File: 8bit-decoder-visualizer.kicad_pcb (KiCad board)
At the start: 2 copper layers, 45 parts, among them SW1 SW_SPDT, SW2 SW_SPDT, SW3 SW_SPDT, SW4 SW_SPDT, SW5 SW_SPDT, SW6 SW_SPDT, SW7 SW_SPDT, SW8 SW_SPDT, U1 LED Display Module, U2 LED Display Module, U3 LED Display Module, U4 LED Display Module, U5 LED Display Module, U6 LED Display Module, U7 74HC595, U8 XIAO_General

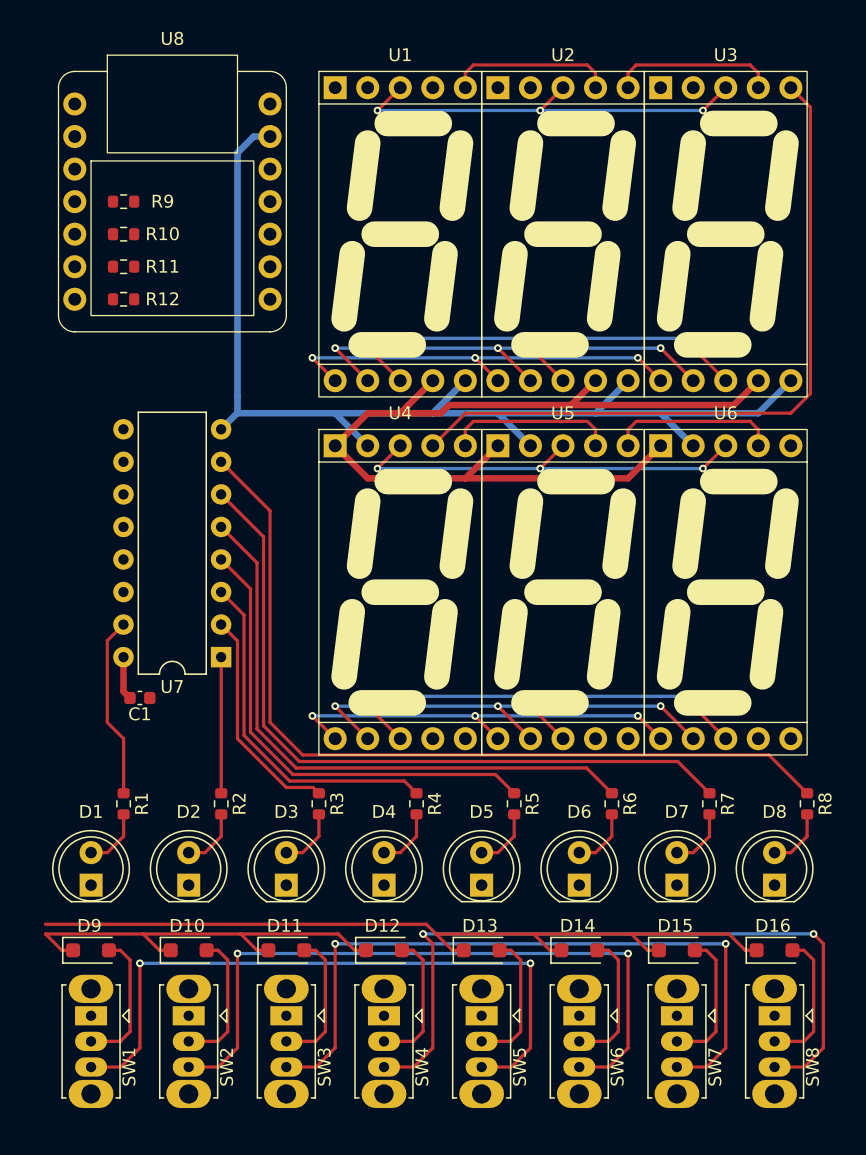
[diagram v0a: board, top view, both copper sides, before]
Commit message: 配線整理
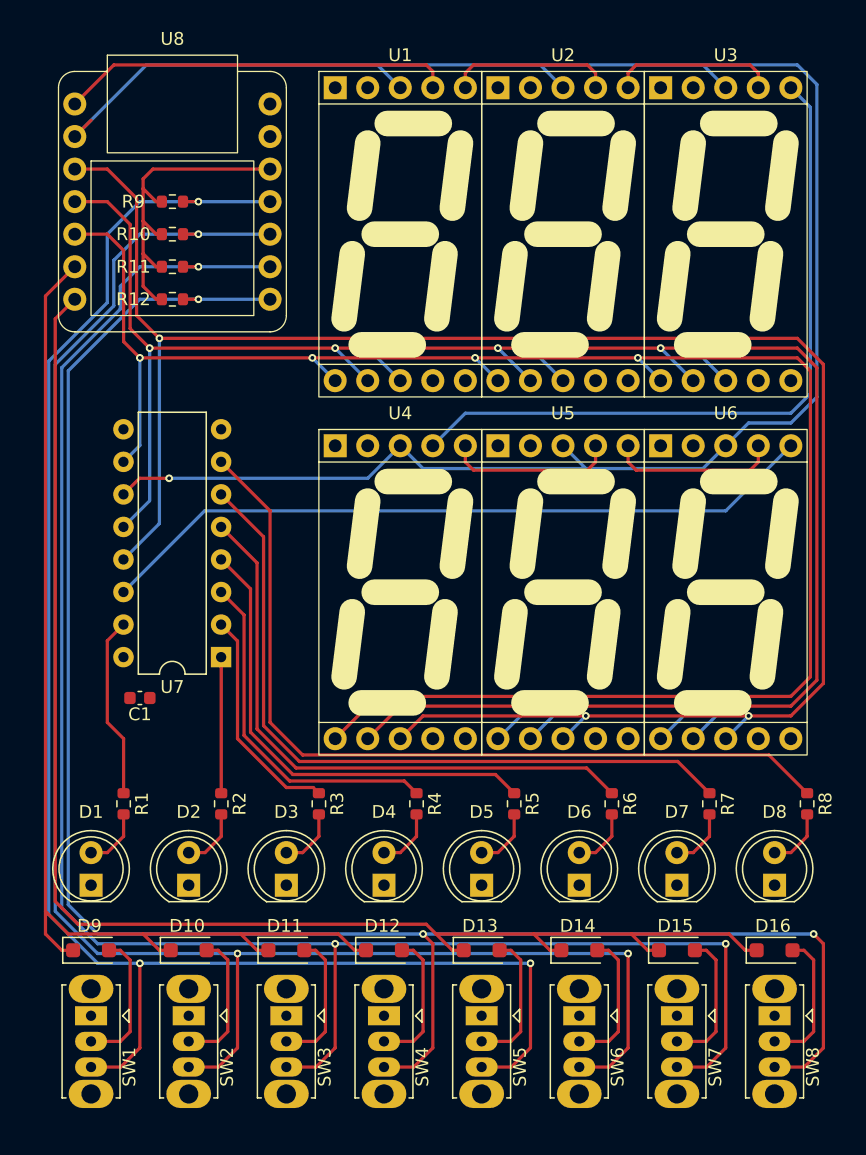
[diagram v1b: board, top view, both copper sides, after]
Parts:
- moved R10 3.81 mm to (127.0, 63.5)
- moved R11 3.81 mm to (127.0, 66.0)
- moved R12 3.81 mm to (127.0, 68.6)
- moved R9 3.81 mm to (127.0, 61.0)
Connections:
- U8 pad 1: unconnected-(U8-GP0-Pad1) -> /LED_SDI
- U8 pad 10: unconnected-(U8-GP9-Pad10) -> /READ_1
- U8 pad 11: unconnected-(U8-GP10-Pad11) -> /READ_0
- U8 pad 2: unconnected-(U8-GP1-Pad2) -> /LED_CLK
- U8 pad 3: unconnected-(U8-GP2-Pad3) -> /LED_EN
- U8 pad 4: unconnected-(U8-GP3-Pad4) -> /LED_LAT
- U8 pad 5: unconnected-(U8-GP4-Pad5) -> /LED_CLR
- U8 pad 6: unconnected-(U8-GP5-Pad6) -> /SCAN_0
- U8 pad 7: unconnected-(U8-GP6-Pad7) -> /SCAN_1
- U8 pad 8: unconnected-(U8-GP7-Pad8) -> /READ_3
- U8 pad 9: unconnected-(U8-GP8-Pad9) -> /READ_2
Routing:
- net /LED_CLK: track 65.9 -> 155.8 mm, vias 6 -> 1
- net /LED_LAT: track 72.4 -> 162.1 mm
- net /READ_3: track 57.7 -> 147.3 mm, vias 2 -> 3
- net /LED_CLR: track 65.9 -> 154.5 mm
- net /LED_EN: track 78.8 -> 167.2 mm
- net GND: track 87.4 -> 0.00 mm
- net /READ_2: track 55.6 -> 142.0 mm, vias 2 -> 3
- net /READ_1: track 54.1 -> 136.6 mm, vias 2 -> 3
- net /READ_0: track 52.5 -> 131.2 mm, vias 2 -> 3
- net Net-(U6-SDO): track 0.00 -> 56.8 mm
- net /SCAN_0: track 33.6 -> 87.3 mm
- net +3V3: track 75.9 -> 26.1 mm
- net /SCAN_1: track 64.4 -> 112.0 mm
- net /LED_SDI: track 0.00 -> 30.7 mm

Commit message: fix AW
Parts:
- moved C1 24.3 mm to (129.8, 75.9)
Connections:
- U1 pad 6: GND -> Net-(U1-GND-Pad6)
- U1 pad 7: +3V3 -> Net-(U1-VDD-Pad7)
- U2 pad 6: GND -> Net-(U2-GND-Pad6)
- U2 pad 7: +3V3 -> Net-(U2-VDD-Pad7)
- U3 pad 6: GND -> Net-(U3-GND-Pad6)
- U3 pad 7: +3V3 -> Net-(U3-VDD-Pad7)
- U4 pad 1: +3V3 -> Net-(U1-VDD-Pad7)
- U4 pad 2: GND -> Net-(U1-GND-Pad6)
- U4 pad 6: GND -> unconnected-(U4-GND-Pad6)
- U4 pad 7: +3V3 -> unconnected-(U4-VDD-Pad7)
- U5 pad 1: +3V3 -> Net-(U2-VDD-Pad7)
- U5 pad 2: GND -> Net-(U2-GND-Pad6)
- U5 pad 6: GND -> unconnected-(U5-GND-Pad6)
- U5 pad 7: +3V3 -> unconnected-(U5-VDD-Pad7)
- U6 pad 1: +3V3 -> Net-(U3-VDD-Pad7)
- U6 pad 2: GND -> Net-(U3-GND-Pad6)
- U6 pad 6: GND -> unconnected-(U6-GND-Pad6)
- U6 pad 7: +3V3 -> unconnected-(U6-VDD-Pad7)
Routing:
- net GND: track 0.00 -> 165.9 mm, vias 0 -> 1
- net +3V3: track 26.1 -> 123.6 mm, vias 0 -> 1
- net Net-(U1-VDD-Pad7): track 0.00 -> 9.72 mm
- net Net-(U1-GND-Pad6): track 0.00 -> 9.72 mm
- net Net-(U3-VDD-Pad7): track 0.00 -> 9.72 mm
- net Net-(U3-GND-Pad6): track 0.00 -> 9.72 mm
- net Net-(U2-VDD-Pad7): track 0.00 -> 9.72 mm
- net Net-(U2-GND-Pad6): track 0.00 -> 9.72 mm

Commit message: 基板外形と寸法線
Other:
- board outline added: 63.5 x 85.1 mm
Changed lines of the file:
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@@
 		)
+	)
+	(gr_rect
+		(start 115.57 48.26)
+		(end 179.07 133.35)
+		(stroke
+			(width 0.05)
+			(type default)
+		)
+		(fill none)
+		(layer "Edge.Cuts")
 	)
 	(gr_text "SW_SPDT"
@@
 		)
 	)
+	(dimension
+		(type aligned)
+		(layer "Cmts.User")
+		(pts
+			(xy 115.57 133.35) (xy 179.07 133.35)
+		)
+		(height 2.54)
+		(gr_text "63.5000 mm"
+			(at 147.32 134.74 0)
+			(layer "Cmts.User")
+			(effects
+				(font
+					(size 1 1)
+					(thickness 0.15)
+				)
+			)
+		)
+		(format
+			(prefix "")
+			(suffix "")
+			(units 3)
+			(units_format 1)
+			(precision 4)
+		)
+		(style
+			(thickness 0.1)
+			(arrow_length 1.27)
+			(text_position_mode 0)
+			(extension_height 0.58642)
+			(extension_offset 0.5) keep_text_aligned)
+	)
+	(dimension
+		(type aligned)
+		(layer "Cmts.User")
+		(pts
+			(xy 179.07 133.35) (xy 179.07 48.26)
+		)
+		(height 2.54)
+		(gr_text "85.0900 mm"
+			(at 180.46 90.805 90)
+			(layer "Cmts.User")
+			(effects
+				(font
+					(size 1 1)
+					(thickness 0.15)
+				)
+			)
+		)
+		(format
+			(prefix "")
+			(suffix "")
+			(units 3)
+			(units_format 1)
+			(precision 4)
+		)
+		(style
+			(thickness 0.1)
+			(arrow_length 1.27)
+			(text_position_mode 0)
+			(extension_height 0.58642)
+			(extension_offset 0.5) keep_text_aligned)
+	)
 	(segment

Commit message: シルク追加
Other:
- board text added: "8bit Decoder Visualizer Rev.1"
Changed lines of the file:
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@@
 		(layer "Edge.Cuts")
+	)
+	(gr_text "8bit Decoder Visualizer\nRev.1"
+		(at 116.84 76.2 270)
+		(layer "F.SilkS")
+		(effects
+			(font
+				(size 1.5 1.5)
+				(thickness 0.25)
+				(bold yes)
+			)
+			(justify left bottom)
+		)
 	)
 	(gr_text "SW_SPDT"

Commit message: 配線手直し
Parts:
- moved C1 3.07 mm to (132.8, 75.7), turned to -90 degrees
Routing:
- net /SCAN_1: track 112.0 -> 115.2 mm
- net GND: track 165.9 -> 163.2 mm, vias 1 -> 0
- net /LED_CLK: track 155.8 -> 154.0 mm, vias 1 -> 0
- net Net-(U5-SDO): track 13.2 -> 11.6 mm
- net Net-(U4-SDO): track 13.2 -> 11.6 mm
- net Net-(U2-SDO): track 13.2 -> 11.6 mm
- net Net-(U1-SDO): track 13.2 -> 11.6 mm
- net +3V3: track 123.6 -> 122.6 mm, vias 1 -> 0
- net /LED_SDI: track 30.7 -> 29.9 mm
